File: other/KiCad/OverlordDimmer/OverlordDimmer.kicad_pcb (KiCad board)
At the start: 2 copper layers, 155.1 x 86.1 mm, 236 parts, among them J1 Connector_Screw_Terminal_01x09, J2 USB_B, J2 USB_cable, J3 DE15_Plug_HighDensity_Mountin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, J4 Connector_Screw_Terminal_01x09, J5 USB_B, J6 Conn_01x12_Pin, Q1 IRF740, Q10 IRF740, Q11 IRF740, Q12 IRF740, Q13 2N3906, Q14 IRF740, Q15 2N3904, Q16 IRF740, Q17 2N3906, Q18 2N3904, Q19 IRF740, Q2 2N3904, Q20 IRF740, Q21 2N7002E, Q22 2N7002E, Q23 2N3904, Q24 IRF740, Q25 IRF740, Q26 2N3904, Q27 IRF740, Q28 IRF740, Q29 2N3906, Q3 2N3906, Q30 2N3904, Q31 2N3906, Q32 IRF740, Q33 2N3906, Q34 2N3904, Q35 IRF740, Q36 IRF740, Q37 2N3904, Q38 2N3906, Q39 IRF740, Q4 IRF740, Q40 IRF740, Q41 2N3906, Q42 IRF740, Q43 2SC4061KT146N, Q44 BC817, Q45 2SC4061KT146N, Q5 IRF740, Q6 2N3906, Q7 2N3904, Q8 2N3904, Q9 2N3906, U1 4N25, U10 4N25, U11 4N25, U12 4N35, U13 LM317_SOT-223, U14 ESP32S3-Wroom, U2 4N25, U3 4N25, U4 SN65HVD230, U5 4N25, U6 4N25, U7 4N25, U8 4N25, U9 4N25

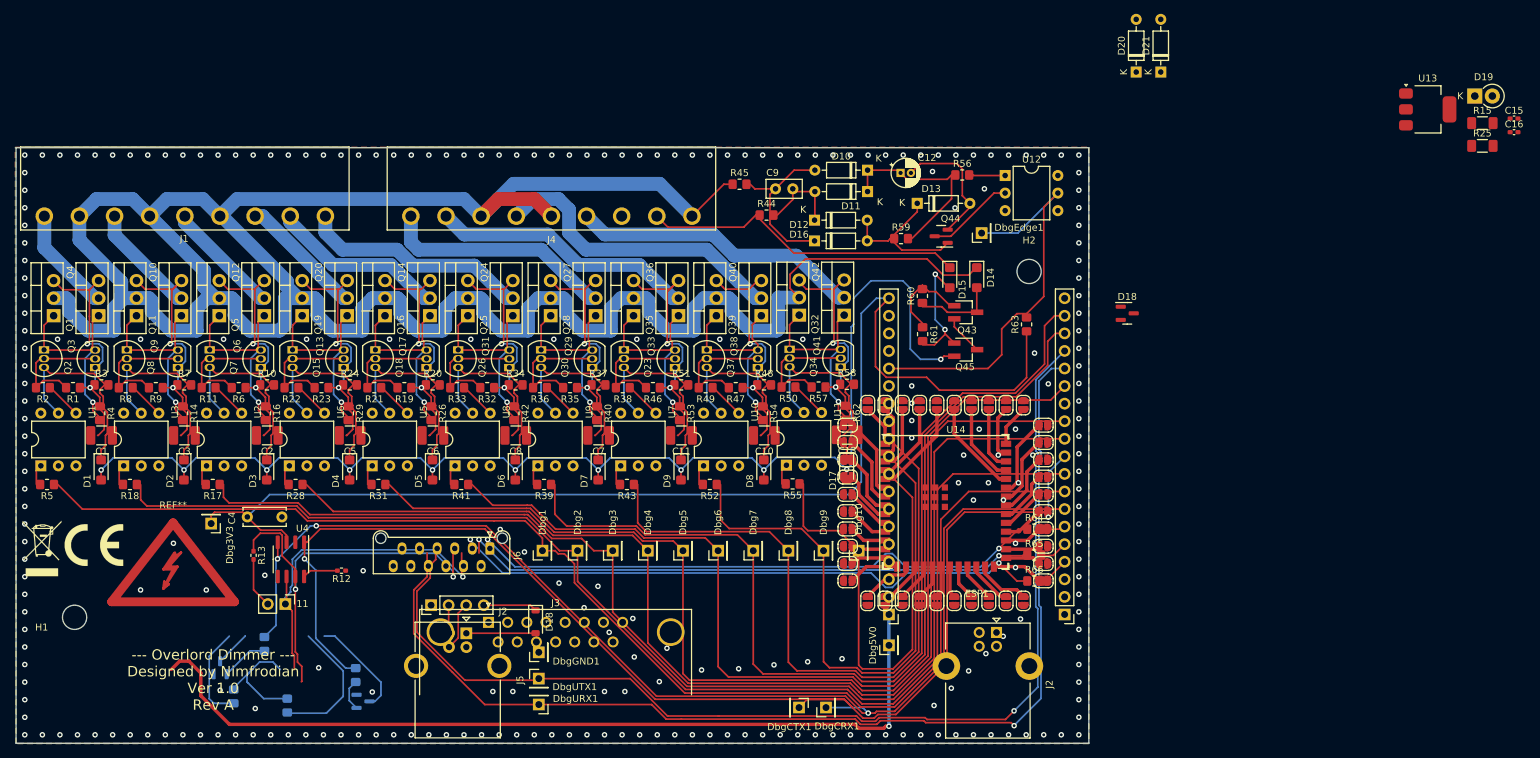
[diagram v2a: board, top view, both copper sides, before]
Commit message: Modified for S3 migration Prepared PCB for final inspection
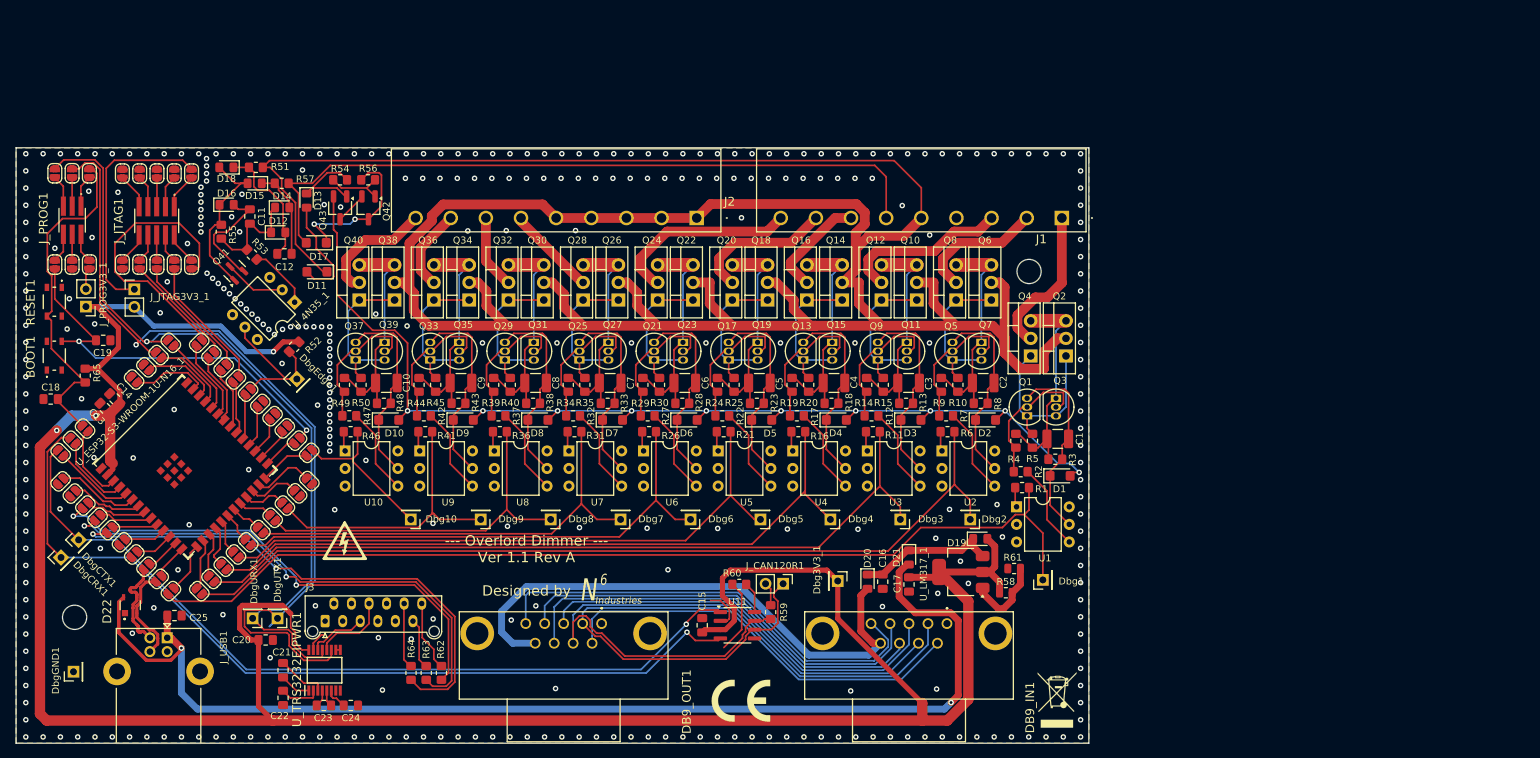
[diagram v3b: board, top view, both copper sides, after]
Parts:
- removed 11: Conn_01x02_Male, Connector_PinHeader_2.54mm:PinHeader_1x02_P2.54mm_Vertical
- removed the D18 at (186.2, 49.5)
- removed the D18 at (100.6, 94.1)
- removed Dbg3V3, Dbg5V0: Connector_Conn_01x01_Male, Connector_PinHeader_2.54mm:PinHeader_1x01_P2.54mm_Vertical
- removed ESP1: ESP-DevKitC-V4, Overlord:ESP32-DevKitC-V4
- removed the J2 at (167.2, 95.6)
- removed the J2 at (85.5, 91.7)
- removed J4: Connector_Screw_Terminal_01x09, TerminalBlockCustom:TerminalBlock_9_5.08mm
- removed J5: USB_B, Connector_USB:USB_B_OST_USB-B1HSxx_Horizontal
- removed J6: Conn_01x12_Pin, Connector_Molex:Molex_Picoflex_90325-0012_2x06_P1.27mm_Vertical
- removed JP1, JP2, JP3: SolderJumper_2_Open, Jumper:SolderJumper-2_P1.3mm_Open_RoundedPad1.0x1.5mm
- removed Q44: BC817, Package_TO_SOT_SMD:SOT-23
- removed Q45: 2SC4061KT146N, Package_TO_SOT_SMD:SC-59_Handsoldering
- removed the R15 at (237.5, 22.0)
- removed the R15 at (57.0, 104.9)
- removed the R25 at (237.5, 25.3)
- removed the R25 at (61.4, 97.3)
- removed R66: 220, Resistor_SMD:R_0805_2012Metric_Pad1.20x1.40mm_HandSolder
- removed REF**: CE-Logo_8.5x6mm_SilkScreen, Symbol:CE-Logo_8.5x6mm_SilkScreen
- removed REF**: Symbol_Highvoltage_Type2_CopperTop_Small, Symbol:Symbol_Highvoltage_Type2_CopperTop_Small
- removed REF**: WEEE-Logo_5.6x8mm_SilkScreen, Symbol:WEEE-Logo_5.6x8mm_SilkScreen
- removed U12: 4N35, Package_DIP:DIP-6_W7.62mm
- removed U13: LM317_SOT-223, Package_TO_SOT_SMD:SOT-223-3_TabPin2
- removed U14: ESP32S3-Wroom, PCM_Espressif:ESP32-S3-WROOM-1U
- added BOOT1: PTS810SJK250SMTR LFS, OverlordCommon:PTS810SJK250SMTRLFS, F.Cu at (31.0, 55.6)
- added C14: 10uF, Capacitor_SMD:C_0805_2012Metric_Pad1.18x1.45mm_HandSolder, F.Cu at (39.8, 61.8)
- added C17: 1uF, Capacitor_SMD:C_0805_2012Metric_Pad1.18x1.45mm_HandSolder, F.Cu at (154.6, 88.7)
- added C18: 0.1uF, Capacitor_SMD:C_0805_2012Metric_Pad1.18x1.45mm_HandSolder, F.Cu at (30.5, 61.9)
- added C19: 0.1uF, Capacitor_SMD:C_0805_2012Metric_Pad1.18x1.45mm_HandSolder, F.Cu at (38.1, 53.4)
- added C20: 0.1uF, Capacitor_SMD:C_0805_2012Metric_Pad1.18x1.45mm_HandSolder, F.Cu at (61.6, 96.7)
- added C21: 0.1uF, Capacitor_SMD:C_0805_2012Metric_Pad1.18x1.45mm_HandSolder, F.Cu at (64.1, 101.1)
- added C22: 0.1uF, Capacitor_SMD:C_0805_2012Metric_Pad1.18x1.45mm_HandSolder, F.Cu at (64.1, 105.1)
- added C23: 0.1uF, Capacitor_SMD:C_0805_2012Metric_Pad1.18x1.45mm_HandSolder, F.Cu at (70.0, 106.2)
- added C24: 0.1uF, Capacitor_SMD:C_0805_2012Metric_Pad1.18x1.45mm_HandSolder, F.Cu at (73.9, 106.2)
- added C25: 0.1uF, Capacitor_SMD:C_0805_2012Metric_Pad1.18x1.45mm_HandSolder, F.Cu at (48.4, 93.2)
- added D18: 1N4148, Diode_SMD:D_0805_2012Metric_Pad1.15x1.40mm_HandSolder, F.Cu at (55.9, 28.4)
- added D22: TPD2E001DZDR, OverlordCommon:TPD2E001DZDR, F.Cu at (42.0, 91.7)
- added DB9_IN1: 5788792-2, OverlordCommon:5788792, F.Cu at (154.6, 101.7)
- added DB9_OUT1: 5747844-4, OverlordCommon:57478444, F.Cu at (104.7, 101.7)
- added Dbg3V3_1: Connector_Conn_01x01_Male, Connector_PinHeader_2.54mm:PinHeader_1x01_P2.54mm_Vertical, F.Cu at (144.3, 88.2)
- added J2: 1757310, OverlordCommon:1757310, F.Cu at (123.9, 35.7)
- added JP41: SolderJumper_2_Open, Jumper:SolderJumper-2_P1.3mm_Open_RoundedPad1.0x1.5mm, F.Cu at (50.9, 29.3)
- added JP42: SolderJumper_2_Open, Jumper:SolderJumper-2_P1.3mm_Open_RoundedPad1.0x1.5mm, F.Cu at (50.9, 42.4)
- added JP43: SolderJumper_2_Open, Jumper:SolderJumper-2_P1.3mm_Open_RoundedPad1.0x1.5mm, F.Cu at (48.4, 29.3)
- added JP44: SolderJumper_2_Open, Jumper:SolderJumper-2_P1.3mm_Open_RoundedPad1.0x1.5mm, F.Cu at (48.4, 42.4)
- added JP45: SolderJumper_2_Open, Jumper:SolderJumper-2_P1.3mm_Open_RoundedPad1.0x1.5mm, F.Cu at (45.9, 29.3)
- added JP46: SolderJumper_2_Open, Jumper:SolderJumper-2_P1.3mm_Open_RoundedPad1.0x1.5mm, F.Cu at (45.9, 42.4)
- added JP47: SolderJumper_2_Open, Jumper:SolderJumper-2_P1.3mm_Open_RoundedPad1.0x1.5mm, F.Cu at (43.4, 29.3)
- added JP48: SolderJumper_2_Open, Jumper:SolderJumper-2_P1.3mm_Open_RoundedPad1.0x1.5mm, F.Cu at (43.4, 42.4)
- added JP49: SolderJumper_2_Open, Jumper:SolderJumper-2_P1.3mm_Open_RoundedPad1.0x1.5mm, F.Cu at (40.9, 29.3)
- added JP50: SolderJumper_2_Open, Jumper:SolderJumper-2_P1.3mm_Open_RoundedPad1.0x1.5mm, F.Cu at (40.9, 42.4)
- added JP51: SolderJumper_2_Open, Jumper:SolderJumper-2_P1.3mm_Open_RoundedPad1.0x1.5mm, F.Cu at (36.1, 29.2)
- added JP52: SolderJumper_2_Open, Jumper:SolderJumper-2_P1.3mm_Open_RoundedPad1.0x1.5mm, F.Cu at (36.1, 42.5)
- added JP53: SolderJumper_2_Open, Jumper:SolderJumper-2_P1.3mm_Open_RoundedPad1.0x1.5mm, F.Cu at (33.6, 29.2)
- added JP54: SolderJumper_2_Open, Jumper:SolderJumper-2_P1.3mm_Open_RoundedPad1.0x1.5mm, F.Cu at (33.6, 42.5)
- added JP55: SolderJumper_2_Open, Jumper:SolderJumper-2_P1.3mm_Open_RoundedPad1.0x1.5mm, F.Cu at (31.1, 29.2)
- added JP56: SolderJumper_2_Open, Jumper:SolderJumper-2_P1.3mm_Open_RoundedPad1.0x1.5mm, F.Cu at (31.1, 42.5)
- added J_CAN120R1: Conn_01x02_Male, Connector_PinHeader_2.54mm:PinHeader_1x02_P2.54mm_Vertical, F.Cu at (136.4, 88.6)
- added J_JTAG1: FTSH-105-01-S-DV-K, OverlordCommon:FTSH-105-XX-YYY-DV-K, F.Cu at (45.8, 36.1)
- added J_JTAG3V3_1: Conn_01x02_Pin, Connector_PinHeader_2.54mm:PinHeader_1x02_P2.54mm_Vertical, F.Cu at (42.6, 46.0)
- added J_PROG1: FTSH-103-01-S-DV-TR, OverlordCommon:FTSH-103-XX-YYY-DV-TR, F.Cu at (33.6, 36.0)
- added J_PROG3V3_1: Conn_01x02_Pin, Connector_PinHeader_2.54mm:PinHeader_1x02_P2.54mm_Vertical, F.Cu at (35.6, 48.5)
- added J_USB1: USB_B, Connector_USB:USB_B_Lumberg_2411_02_Horizontal, F.Cu at (47.4, 96.4)
- added R15: 470k, Resistor_SMD:R_0805_2012Metric_Pad1.20x1.40mm_HandSolder, F.Cu at (150.9, 59.8)
- added R25: 470k, Resistor_SMD:R_0805_2012Metric_Pad1.20x1.40mm_HandSolder, F.Cu at (129.3, 59.8)
- added RESET1: PTS810SJK250SMTR LFS, OverlordCommon:PTS810SJK250SMTRLFS, F.Cu at (31.0, 47.8)
- added SYM1: HV_symbol, OverlordCommon:HV_symbol, B.Cu at (160.8, 30.6)
- added SYM2: N6_logo_medium, OverlordCommon:Symbol_N6Industries_medium, B.Cu at (172.6, 106.3)
- added SYM3: CE, Symbol:CE-Logo_8.5x6mm_SilkScreen, F.Cu at (130.3, 105.5)
- added SYM4: WEEE, Symbol:WEEE-Logo_5.6x8mm_SilkScreen, F.Cu at (176.0, 105.4)
- added SYM5: N6_logo_medium, OverlordCommon:Symbol_N6Industries_medium, F.Cu at (111.7, 89.9)
- added SYM6: HV_symbol, OverlordCommon:HV_symbol, F.Cu at (73.0, 82.7)
- added U_4N35_1: 4N35, Package_DIP:DIP-6_W7.62mm, F.Cu at (65.8, 47.9)
- added U_ESP32-S3-WROOM-1U-N16_1: ESP32S3-Wroom, PCM_Espressif:ESP32-S3-WROOM-1U, F.Cu at (49.8, 71.6)
- added U_LM317_1: LM317_SOT-223, Package_TO_SOT_SMD:SOT-223-3_TabPin2, F.Cu at (162.1, 86.9)
- added U_TRS3232EIPWR1: TRS3232EIPWR, OverlordCommon:SOP65P640X120-16N, F.Cu at (70.1, 101.1)
- C11: value 4.7u -> 10uF; footprint Capacitor_SMD:C_1210_3225Metric_Pad1.33x2.70mm_HandSolder -> Capacitor_SMD:C_0805_2012Metric_Pad1.18x1.45mm_HandSolder
- C12: value 10uF -> 1nF; footprint Capacitor_THT:CP_Radial_D4.0mm_P1.50mm -> Capacitor_SMD:C_0805_2012Metric_Pad1.18x1.45mm_HandSolder
- C13: value 4.7u -> 0.1uF; footprint Capacitor_SMD:C_1210_3225Metric_Pad1.33x2.70mm_HandSolder -> Capacitor_SMD:C_0805_2012Metric_Pad1.18x1.45mm_HandSolder
- C15: value 1uF -> 0.1uF; footprint Capacitor_SMD:C_0402_1005Metric_Pad0.74x0.62mm_HandSolder -> Capacitor_SMD:C_0805_2012Metric_Pad1.18x1.45mm_HandSolder
- C16: footprint Capacitor_SMD:C_0402_1005Metric_Pad0.74x0.62mm_HandSolder -> Capacitor_SMD:C_0805_2012Metric_Pad1.18x1.45mm_HandSolder
- C4: value 100nF -> 4.7u; footprint Capacitor_THT:C_Disc_D6.0mm_W2.5mm_P5.00mm -> Capacitor_SMD:C_1210_3225Metric_Pad1.33x2.70mm_HandSolder
- C9: value 1nF -> 4.7u; footprint Capacitor_THT:C_Disc_D5.0mm_W2.5mm_P2.50mm -> Capacitor_SMD:C_1210_3225Metric_Pad1.33x2.70mm_HandSolder
- D10, D11: value 1N4148 -> VISHAY S07J-GS08; footprint Diode_THT:D_DO-35_SOD27_P7.62mm_Horizontal -> Diode_SMD:D_SMF
- D12, D16, D20, D21: footprint Diode_THT:D_DO-35_SOD27_P7.62mm_Horizontal -> Diode_SMD:D_0805_2012Metric_Pad1.15x1.40mm_HandSolder
- D13: value 1N4148 -> Unknown; footprint Diode_THT:D_DO-35_SOD27_P7.62mm_Horizontal -> Diode_SMD:D_0805_2012Metric_Pad1.15x1.40mm_HandSolder
- D14, D15: value VISHAY S07J-GS08 -> 1N4148; footprint Diode_SMD:D_SMF -> Diode_SMD:D_0805_2012Metric_Pad1.15x1.40mm_HandSolder
- D19: value 1N4002 -> 1N4148; footprint Diode_THT:D_DO-41_SOD81_P2.54mm_Vertical_KathodeUp -> Diode_SMD:D_0805_2012Metric_Pad1.15x1.40mm_HandSolder
- J1: value Connector_Screw_Terminal_01x09 -> 1757310; footprint TerminalBlockCustom:TerminalBlock_9_5.08mm -> OverlordCommon:1757310
- J3: value DE15_Plug_HighDensity_MountingHoles -> Conn_01x12_Pin; footprint Connector_Dsub:DSUB-15_Male_Horizontal_P2.77x2.84mm_EdgePinOffset7.70mm_Housed_MountingHolesOffset9.12mm -> Connector_Molex:Molex_Picoflex_90325-0012_2x06_P1.27mm_Vertical
- Q1, Q25, Q5: value IRF740 -> 2N3904; footprint Package_TO_SOT_THT:TO-220-3_Vertical -> Package_TO_SOT_THT:TO-92_Inline
- Q11, Q19, Q27, Q35, Q39: value IRF740 -> 2N3906; footprint Package_TO_SOT_THT:TO-220-3_Vertical -> Package_TO_SOT_THT:TO-92_Inline
- Q13, Q17, Q29, Q33, Q9: value 2N3906 -> 2N3904
- Q15, Q23, Q7: value 2N3904 -> 2N3906
- Q18, Q2, Q26, Q30, Q34, Q8: value 2N3904 -> IRF740; footprint Package_TO_SOT_THT:TO-92_Inline -> Package_TO_SOT_THT:TO-220-3_Vertical
- Q21: value 2N7002E -> 2N3904; footprint Package_TO_SOT_SMD:SOT-23 -> Package_TO_SOT_THT:TO-92_Inline; moved to F.Cu
- Q22: value 2N7002E -> IRF740; footprint Package_TO_SOT_SMD:SOT-23 -> Package_TO_SOT_THT:TO-220-3_Vertical; moved to F.Cu
- Q38, Q6: value 2N3906 -> IRF740; footprint Package_TO_SOT_THT:TO-92_Inline -> Package_TO_SOT_THT:TO-220-3_Vertical
- Q41: value 2N3906 -> BC817; footprint Package_TO_SOT_THT:TO-92_Inline -> Package_TO_SOT_SMD:SOT-23
- Q42: value IRF740 -> 2SC4061KT146N; footprint Package_TO_SOT_THT:TO-220-3_Vertical -> Package_TO_SOT_SMD:SC-59_Handsoldering
- R1, R46, R6: value 10k -> 220
- R11, R21, R36: value 1k -> 220
- R12: value 20K -> 1k; footprint Resistor_SMD:R_0402_1005Metric_Pad0.72x0.64mm_HandSolder -> Resistor_SMD:R_0805_2012Metric_Pad1.20x1.40mm_HandSolder
- R13: value 120 -> 470k; footprint Resistor_SMD:R_0402_1005Metric_Pad0.72x0.64mm_HandSolder -> Resistor_SMD:R_0805_2012Metric_Pad1.20x1.40mm_HandSolder
- R14, R24, R29, R34, R4: value 470k -> 10k
- R16, R26, R62: value 470k -> 220
- R17: value 220 -> 1k
- R18, R28, R43, R5: value 220 -> 470k
- R23, R35: value 10k -> 470k
- R27: value 5K -> 1k; moved to F.Cu
- R30: value 10K -> 470k; moved to F.Cu
- R32, R47: value 10k -> 1k
- R33, R38, R50, R8: value 1k -> 470k
- R37, R42, R53, R7: value 470k -> 1k
- R39, R65: value 220 -> 10k
- R44: value 220k -> 10k
- R45: value 220k -> 470k
- R49: value 1k -> 10k
- R51: value 470k -> 220k
- R52: value 220 -> 2.2k
- R54: value 470k -> 100k
- R55: value 220 -> 22k
- R56: value 1k -> 75k
- R57: value 10k -> 220k
- R58: value 470k -> 240; footprint Resistor_SMD:R_0805_2012Metric_Pad1.20x1.40mm_HandSolder -> Resistor_SMD:R_0805_2012Metric
- R59: value 22k -> 120
- R60: value 75k -> 0R
- R61: value 100k -> 390; footprint Resistor_SMD:R_0805_2012Metric_Pad1.20x1.40mm_HandSolder -> Resistor_SMD:R_0805_2012Metric
- R63: value 2.2k -> 220
- U11: value 4N25 -> SN65HVD230; footprint Package_DIP:DIP-6_W7.62mm -> Package_SO:SOIC-8_3.9x4.9mm_P1.27mm
- U4: value SN65HVD230 -> 4N25; footprint Package_SO:SOIC-8_3.9x4.9mm_P1.27mm -> Package_DIP:DIP-6_W7.62mm
- moved Q2 147.8 mm to (177.3, 55.7), turned to 90 degrees
- moved R5 142.6 mm to (172.4, 67.9), turned to 90 degrees
- moved JP11 142.2 mm to (31.9, 73.8), turned to -135 degrees
- moved JP9 142.1 mm to (31.9, 69.7), turned to 135 degrees
- moved R2 141.9 mm to (170.8, 72.4)
- moved Q1 141.5 mm to (171.7, 64.3)
- moved U1 141.2 mm to (170.2, 77.5), turned to 0 degrees
- moved JP13 140.5 mm to (33.7, 75.6), turned to -135 degrees
- moved JP7 140.3 mm to (33.7, 67.9), turned to 135 degrees
- moved R65 139.6 mm to (35.5, 58.5), turned to 90 degrees
- moved Q3 139.0 mm to (175.8, 61.8), turned to -90 degrees
- moved D1 138.7 mm to (176.4, 73.0), turned to 0 degrees
- moved C15 138.4 mm to (124.7, 94.6), turned to 90 degrees
- moved R3 138.3 mm to (175.8, 70.6)
- moved C1 138.3 mm to (176.1, 67.7)
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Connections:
- C1 pad 2: Net-(Q1-S) -> Net-(Q2-S)
- C10 pad 1: Net-(D8-K) -> Net-(D10-K)
- C10 pad 2: Net-(Q38-E) -> Net-(Q38-S)
- C11 pad 1: Net-(D9-K) -> Net-(D12-K)
- C11 pad 2: Net-(Q33-E) -> Net-(D16-A)
- C12 pad 1: Net-(D10-K) -> Net-(D12-A)
- C12 pad 2: Net-(D13-A) -> Net-(D14-A)
- C13 pad 1: Net-(D17-K) -> +3.3V
- C13 pad 2: Net-(Q32-S) -> GND
- C15 pad 1: Net-(D19-K) -> +3.3V
- C16 pad 1: +3.3V -> Net-(D19-K)
- C2 pad 1: Net-(D3-K) -> Net-(D2-K)
- C2 pad 2: Net-(Q12-S) -> Net-(Q6-S)
- C3 pad 1: Net-(D2-K) -> Net-(D3-K)
- C4 pad 1: GND -> Net-(D4-K)
- C4 pad 2: +3.3V -> Net-(Q14-S)
- C5 pad 1: Net-(D4-K) -> Net-(D5-K)
- C5 pad 2: Net-(Q13-E) -> Net-(Q18-S)
- C6 pad 1: Net-(D5-K) -> Net-(D6-K)
- C6 pad 2: Net-(Q14-S) -> Net-(Q22-S)
- C7 pad 2: Net-(Q27-S) -> Net-(Q26-S)
- C8 pad 1: Net-(D6-K) -> Net-(D8-K)
- C8 pad 2: Net-(Q24-S) -> Net-(Q30-S)
- C9 pad 1: Net-(D10-A) -> Net-(D9-K)
- C9 pad 2: Net-(D11-A) -> Net-(Q34-S)
- D10 pad 2: Net-(D10-A) -> VCC
- D11 pad 1: Net-(D10-K) -> L
- D12 pad 1: Net-(D11-A) -> Net-(D12-K)
- D13 pad 1: Net-(D12-A) -> Net-(D13-K)
- D13 pad 2: Net-(D13-A) -> Net-(D11-A)
- D14 pad 1: L -> Net-(D12-K)
- D15 pad 1: Net-(D15-K) -> Net-(D14-A)
- D15 pad 2: N -> Net-(D15-A)
- D16 pad 1: Net-(D10-A) -> Net-(D15-A)
- D16 pad 2: Net-(D12-A) -> Net-(D16-A)
- D17 pad 2: VCC -> N
- J1 pad 1: /Load -> OUT1
- J1 pad 2: /Load_8 -> OUT2
- J1 pad 3: /Load_6 -> OUT3
- J1 pad 4: unconnected-(J1-Pin_4-Pad4) -> GND
- J1 pad 5: /Load_7 -> L
- J1 pad 6: unconnected-(J1-Pin_6-Pad6) -> N
- J1 pad 7: /Load_5 -> OUT4
- J1 pad 8: unconnected-(J1-Pin_8-Pad8) -> OUT5
- J1 pad 9: /Load_9 -> OUT6
- J3 pad 1: GND -> unconnected-(J3-Pin_1-Pad1)
- J3 pad 10: unconnected-(J3-Pad10) -> Net-(J3-Pin_10)
- J3 pad 11: CAN_H -> Net-(J3-Pin_11)
- J3 pad 12: MB1_H -> Net-(J3-Pin_12)
- J3 pad 2: MB1_L -> unconnected-(J3-Pin_2-Pad2)
- J3 pad 5: unconnected-(J3-Pad5) -> RS232_TX
- J3 pad 6: GND -> RS232_RX
- J3 pad 7: CAN_L -> GND
- J3 pad 8: MB2_L -> unconnected-(J3-Pin_8-Pad8)
- JP10 pad 2: unconnected-(JP10-B-Pad2) -> UART_RX_0
- JP12 pad 2: unconnected-(JP12-B-Pad2) -> JTAG_TMS
- JP14 pad 2: unconnected-(JP14-B-Pad2) -> JTAG_TDI
- JP15 pad 2: unconnected-(JP15-B-Pad2) -> STATUS_LED_R
- JP16 pad 2: unconnected-(JP16-B-Pad2) -> JTAG_TDO
- JP17 pad 2: unconnected-(JP17-B-Pad2) -> STATUS_LED_G
- JP18 pad 2: unconnected-(JP18-B-Pad2) -> JTAG_TCK
- JP19 pad 2: unconnected-(JP19-B-Pad2) -> STATUS_LED_B
- JP20 pad 2: unconnected-(JP20-B-Pad2) -> EDGE_DETECT
- JP25 pad 2: unconnected-(JP25-B-Pad2) -> D-
- JP27 pad 2: unconnected-(JP27-B-Pad2) -> D+
- JP28 pad 2: unconnected-(JP28-B-Pad2) -> ESP_IO0
- JP29 pad 2: unconnected-(JP29-B-Pad2) -> TRGR1
- JP30 pad 2: unconnected-(JP30-B-Pad2) -> TRGR2
- JP31 pad 2: unconnected-(JP31-B-Pad2) -> TRGR3
- JP32 pad 2: unconnected-(JP32-B-Pad2) -> TRGR4
- JP33 pad 2: unconnected-(JP33-B-Pad2) -> TRGR5
- JP34 pad 2: unconnected-(JP34-B-Pad2) -> TRGR6
- JP35 pad 2: unconnected-(JP35-B-Pad2) -> TRGR7
- JP36 pad 2: unconnected-(JP36-B-Pad2) -> TRGR8
- JP37 pad 2: unconnected-(JP37-B-Pad2) -> TRGR9
- JP40 pad 2: unconnected-(JP40-B-Pad2) -> TRGR10
- JP5 pad 2: unconnected-(JP5-B-Pad2) -> ESP_EN
- JP7 pad 2: unconnected-(JP7-B-Pad2) -> CAN_RX
- JP8 pad 2: unconnected-(JP8-B-Pad2) -> UART_TX_0
- JP9 pad 2: unconnected-(JP9-B-Pad2) -> CAN_TX
- Q1 pad 1: Net-(Q1-G) -> Net-(Q1-E)
- Q1 pad 2: L -> Net-(Q1-B)
- Q1 pad 3: Net-(Q1-S) -> Net-(D1-K)
- Q10 pad 2: Load -> L
- Q11 pad 1: Net-(Q10-G) -> Net-(Q10-S)
- Q11 pad 2: L -> Net-(Q11-B)
- Q11 pad 3: Net-(Q10-S) -> Net-(Q10-G)
- Q12 pad 1: Net-(Q12-G) -> Net-(Q10-G)
- Q12 pad 2: Load -> OUT3
- Q12 pad 3: Net-(Q12-S) -> Net-(Q10-S)
- Q13 pad 3: Net-(Q13-C) -> Net-(D4-K)
- Q14 pad 1: Net-(Q14-G) -> Net-(Q13-E)
- Q14 pad 2: Load -> L
- Q15 pad 1: Net-(Q13-C) -> Net-(Q14-S)
- Q15 pad 3: Net-(D4-K) -> Net-(Q13-E)
- Q16 pad 1: Net-(Q14-G) -> Net-(Q13-E)
- Q16 pad 2: L -> OUT4
- Q17 pad 1: Net-(Q14-S) -> Net-(Q17-E)
- Q17 pad 3: Net-(Q14-G) -> Net-(D5-K)
- Q18 pad 1: Net-(Q14-G) -> Net-(Q17-E)
- Q18 pad 2: Net-(Q17-B) -> L
- Q18 pad 3: Net-(D5-K) -> Net-(Q18-S)
- Q19 pad 1: Net-(Q13-C) -> Net-(Q18-S)
- Q19 pad 2: L -> Net-(Q17-B)
- Q19 pad 3: Net-(Q13-E) -> Net-(Q17-E)
- Q2 pad 1: Net-(Q1-G) -> Net-(Q1-E)
- Q2 pad 2: Net-(Q2-B) -> L
- Q2 pad 3: Net-(D1-K) -> Net-(Q2-S)
- Q20 pad 1: Net-(Q13-C) -> Net-(Q17-E)
- Q20 pad 2: Load -> OUT5
- Q20 pad 3: Net-(Q13-E) -> Net-(Q18-S)
- Q21 pad 1: Net-(Q21-G) -> Net-(Q21-E)
- Q21 pad 2: GND -> Net-(Q21-B)
- Q21 pad 3: Net-(Q21-D) -> Net-(D6-K)
- Q22 pad 1: Net-(Q22-G) -> Net-(Q21-E)
- Q22 pad 2: GND -> L
- Q22 pad 3: Net-(Q22-D) -> Net-(Q22-S)
- Q23 pad 1: Net-(Q23-E) -> Net-(Q22-S)
- Q23 pad 2: Net-(Q23-B) -> Net-(Q21-B)
- Q23 pad 3: Net-(D9-K) -> Net-(Q21-E)
- Q24 pad 1: Net-(Q24-G) -> Net-(Q21-E)
- Q24 pad 2: Load -> OUT6
- Q24 pad 3: Net-(Q24-S) -> Net-(Q22-S)
- Q25 pad 1: Net-(Q24-G) -> Net-(Q25-E)
- Q25 pad 2: L -> Net-(Q25-B)
- Q25 pad 3: Net-(Q24-S) -> Net-(D7-K)
- Q26 pad 1: Net-(Q24-G) -> Net-(Q25-E)
- Q26 pad 2: Net-(Q26-B) -> L
- Q26 pad 3: Net-(D6-K) -> Net-(Q26-S)
- Q27 pad 1: Net-(Q27-G) -> Net-(Q26-S)
- Q27 pad 2: Load -> Net-(Q25-B)
- Q27 pad 3: Net-(Q27-S) -> Net-(Q25-E)
- Q28 pad 1: Net-(Q27-G) -> Net-(Q25-E)
- Q28 pad 2: L -> OUT7
- Q28 pad 3: Net-(Q27-S) -> Net-(Q26-S)
- Q29 pad 1: Net-(Q27-S) -> Net-(Q29-E)
- Q29 pad 3: Net-(Q27-G) -> Net-(D8-K)
- Q3 pad 1: Net-(Q1-S) -> Net-(Q2-S)
- Q3 pad 2: Net-(Q2-B) -> Net-(Q1-B)
- Q3 pad 3: Net-(Q1-G) -> Net-(Q1-E)
- Q30 pad 1: Net-(Q27-G) -> Net-(Q29-E)
- Q30 pad 2: Net-(Q29-B) -> L
- Q30 pad 3: Net-(D7-K) -> Net-(Q30-S)
- Q31 pad 1: Net-(Q24-S) -> Net-(Q30-S)
- Q31 pad 2: Net-(Q26-B) -> Net-(Q29-B)
- Q31 pad 3: Net-(Q24-G) -> Net-(Q29-E)
- Q32 pad 1: Net-(Q32-G) -> Net-(Q29-E)
- Q32 pad 2: L -> OUT8
- Q32 pad 3: Net-(Q32-S) -> Net-(Q30-S)
- Q33 pad 2: Net-(Q23-B) -> Net-(Q33-B)
- Q33 pad 3: Net-(Q23-E) -> Net-(D9-K)
- Q34 pad 1: Net-(Q32-G) -> Net-(Q33-E)
- Q34 pad 2: Net-(Q34-B) -> L
- Q34 pad 3: Net-(D17-K) -> Net-(Q34-S)
- Q35 pad 1: Net-(Q23-E) -> Net-(Q34-S)
- Q35 pad 2: L -> Net-(Q33-B)
- Q36 pad 1: Net-(Q23-E) -> Net-(Q33-E)
- Q36 pad 2: Load -> OUT9
- Q36 pad 3: Net-(Q33-E) -> Net-(Q34-S)
- Q37 pad 3: Net-(D8-K) -> Net-(D10-K)
- Q38 pad 1: Net-(Q38-E) -> Net-(Q37-E)
- Q38 pad 2: Net-(Q37-B) -> L
- Q38 pad 3: Net-(Q37-E) -> Net-(Q38-S)
- Q39 pad 1: Net-(Q37-E) -> Net-(Q38-S)
- Q39 pad 2: L -> Net-(Q37-B)
- Q39 pad 3: Net-(Q38-E) -> Net-(Q37-E)
- Q4 pad 1: Net-(Q1-G) -> Net-(Q1-E)
- Q4 pad 2: Load -> OUT1
- Q4 pad 3: Net-(Q1-S) -> Net-(Q2-S)
- Q40 pad 2: Load -> OUT10
- Q40 pad 3: Net-(Q38-E) -> Net-(Q38-S)
- Q41 pad 1: Net-(Q32-S) -> Net-(D15-A)
- Q41 pad 2: Net-(Q34-B) -> Net-(D16-A)
- Q41 pad 3: Net-(Q32-G) -> Net-(Q41-C)
- Q42 pad 1: Net-(Q32-G) -> Net-(Q42-B)
- Q42 pad 2: Load -> Net-(Q42-E)
- Q42 pad 3: Net-(Q32-S) -> Net-(D17-K)
- Q43 pad 1: Net-(Q43-B) -> Net-(D13-K)
- Q43 pad 2: Net-(Q43-E) -> VCC
- Q43 pad 3: Net-(D15-K) -> Net-(Q42-E)
- Q5 pad 1: Net-(Q12-G) -> Net-(Q5-E)
- Q5 pad 2: L -> Net-(Q5-B)
- Q5 pad 3: Net-(Q12-S) -> Net-(D2-K)
- Q6 pad 1: Net-(Q12-S) -> Net-(Q5-E)
- Q6 pad 2: Net-(Q6-B) -> L
- Q6 pad 3: Net-(Q12-G) -> Net-(Q6-S)
- Q7 pad 1: Net-(Q12-G) -> Net-(Q6-S)
- Q7 pad 2: Net-(Q6-B) -> Net-(Q5-B)
- Q7 pad 3: Net-(D3-K) -> Net-(Q5-E)
- Q8 pad 1: Net-(Q10-G) -> Net-(Q5-E)
- Q8 pad 2: Net-(Q8-B) -> OUT2
- Q8 pad 3: Net-(D2-K) -> Net-(Q6-S)
- Q9 pad 1: Net-(Q10-S) -> Net-(Q10-G)
- Q9 pad 2: Net-(Q8-B) -> Net-(Q11-B)
- Q9 pad 3: Net-(Q10-G) -> Net-(D3-K)
- R1 pad 1: Net-(Q1-S) -> TRGR1
- R1 pad 2: Net-(Q2-B) -> Net-(R1-Pad2)
- R10 pad 1: Net-(Q12-S) -> Net-(Q6-S)
- R10 pad 2: Net-(D3-K) -> Net-(Q5-E)
- R11 pad 1: Net-(R11-Pad1) -> TRGR3
- R11 pad 2: Net-(Q6-B) -> Net-(R11-Pad2)
- R12 pad 1: GND -> Net-(R12-Pad1)
- R12 pad 2: Net-(U4-Rs) -> Net-(Q11-B)
- R13 pad 1: CAN_H -> Net-(Q10-S)
- R13 pad 2: Net-(11-Pin_2) -> Net-(D3-K)
- R14 pad 2: Net-(Q10-G) -> Net-(Q11-B)
- R16 pad 1: Net-(Q12-S) -> TRGR4
- R16 pad 2: Net-(Q12-G) -> Net-(R16-Pad2)
- R17 pad 1: TRGR3 -> Net-(R17-Pad1)
- R17 pad 2: Net-(R17-Pad2) -> Net-(Q13-B)
- R18 pad 1: TRGR2 -> Net-(Q14-S)
- R18 pad 2: Net-(R18-Pad2) -> Net-(D4-K)
- R19 pad 2: Net-(Q17-B) -> Net-(Q13-B)
- R2 pad 2: Net-(Q2-B) -> Net-(Q1-B)
- R20 pad 2: Net-(D5-K) -> Net-(Q13-E)
- R21 pad 1: Net-(R21-Pad1) -> TRGR5
- R21 pad 2: Net-(Q17-B) -> Net-(R21-Pad2)
- R22 pad 2: Net-(Q13-B) -> Net-(Q17-B)
- R23 pad 1: Net-(Q13-E) -> Net-(Q18-S)
- R23 pad 2: Net-(Q13-B) -> Net-(D5-K)
- R24 pad 1: Net-(Q13-E) -> Net-(Q18-S)
- R24 pad 2: Net-(D4-K) -> Net-(Q17-B)
- R26 pad 1: Net-(Q14-S) -> TRGR6
- R26 pad 2: Net-(Q14-G) -> Net-(R26-Pad2)
- R27 pad 1: Net-(J3-Pad10) -> Net-(R27-Pad1)
- R27 pad 2: +12V -> Net-(Q21-B)
- R28 pad 1: TRGR4 -> Net-(Q22-S)
- R28 pad 2: Net-(R28-Pad2) -> Net-(D6-K)
- R29 pad 1: Net-(Q13-E) -> Net-(Q22-S)
- R29 pad 2: Net-(Q13-C) -> Net-(Q21-B)
- R3 pad 1: Net-(Q1-S) -> Net-(Q2-S)
- R30 pad 1: Net-(Q21-G) -> Net-(Q22-S)
- R30 pad 2: CAN_TX -> Net-(Q21-E)
- R31 pad 1: TRGR5 -> TRGR7
- R32 pad 1: Net-(Q24-S) -> Net-(R32-Pad1)
- R32 pad 2: Net-(Q26-B) -> Net-(Q25-B)
- R33 pad 1: Net-(R33-Pad1) -> Net-(Q26-S)
- R33 pad 2: Net-(Q26-B) -> Net-(D7-K)
- R34 pad 1: Net-(Q24-S) -> Net-(Q26-S)
- R34 pad 2: Net-(D6-K) -> Net-(Q25-B)
- R35 pad 1: Net-(Q27-S) -> Net-(Q26-S)
- R35 pad 2: Net-(Q29-B) -> Net-(Q25-E)
- R36 pad 1: Net-(R36-Pad1) -> TRGR8
- R36 pad 2: Net-(Q29-B) -> Net-(R36-Pad2)
- R37 pad 1: Net-(Q27-S) -> Net-(R37-Pad1)
- R37 pad 2: Net-(D7-K) -> Net-(Q29-B)
- R38 pad 1: Net-(R38-Pad1) -> Net-(Q30-S)
- R38 pad 2: Net-(Q23-B) -> Net-(D8-K)
- R39 pad 1: TRGR7 -> Net-(Q30-S)
- R39 pad 2: Net-(R39-Pad2) -> Net-(Q29-B)
- R4 pad 1: Net-(Q1-S) -> Net-(Q2-S)
- R4 pad 2: Net-(Q1-G) -> Net-(Q1-B)
- R40 pad 1: Net-(Q27-S) -> Net-(Q30-S)
- R40 pad 2: Net-(Q27-G) -> Net-(Q29-E)
- R41 pad 1: TRGR6 -> TRGR9
- R42 pad 1: Net-(Q24-S) -> Net-(R42-Pad1)
- R42 pad 2: Net-(Q24-G) -> Net-(Q33-B)
- R43 pad 1: TRGR8 -> Net-(Q34-S)
- R43 pad 2: Net-(R43-Pad2) -> Net-(D9-K)
- R44 pad 1: N -> Net-(Q34-S)
- R44 pad 2: Net-(D11-A) -> Net-(Q33-B)
- R45 pad 1: L -> Net-(Q34-S)
- R45 pad 2: Net-(D10-A) -> Net-(Q33-E)
- R46 pad 1: Net-(Q33-E) -> TRGR10
- R46 pad 2: Net-(Q23-B) -> Net-(R46-Pad2)
- R47 pad 1: Net-(Q38-E) -> Net-(R47-Pad1)
- R48 pad 1: Net-(Q38-E) -> Net-(Q38-S)
- R48 pad 2: Net-(D8-K) -> Net-(D10-K)
- R49 pad 1: Net-(R49-Pad1) -> Net-(Q38-S)
- R5 pad 1: TRGR1 -> Net-(Q2-S)
- R5 pad 2: Net-(R5-Pad2) -> Net-(Q1-E)
- R50 pad 1: Net-(R50-Pad1) -> Net-(Q38-S)
- R50 pad 2: Net-(Q34-B) -> Net-(Q37-E)
- R51 pad 1: Net-(Q33-E) -> L
- R51 pad 2: Net-(D9-K) -> Net-(D12-A)
- R52 pad 1: TRGR9 -> +3.3V
- R52 pad 2: Net-(R52-Pad2) -> EDGE_DETECT
- R53 pad 1: Net-(Q33-E) -> Net-(D12-K)
- R53 pad 2: Net-(Q23-E) -> Net-(R53-Pad2)
- R54 pad 1: Net-(Q38-E) -> Net-(D13-K)
- R54 pad 2: Net-(Q37-E) -> Net-(Q42-B)
- R55 pad 1: TRGR10 -> Net-(D15-A)
- R55 pad 2: Net-(R55-Pad2) -> Net-(D12-K)
- R56 pad 1: Net-(D10-K) -> Net-(Q42-B)
- R56 pad 2: Net-(R56-Pad2) -> Net-(D17-K)
- R57 pad 1: Net-(Q32-S) -> N
- R57 pad 2: Net-(Q34-B) -> Net-(D14-A)
- R58 pad 1: Net-(Q32-S) -> +3.3V
- R58 pad 2: Net-(D17-K) -> Net-(U_LM317_1-ADJ)
- R59 pad 1: Net-(D12-A) -> CAN_H
- R59 pad 2: Net-(D10-K) -> Net-(J_CAN120R1-Pin_2)
- R6 pad 1: Net-(Q12-S) -> TRGR2
- R6 pad 2: Net-(Q6-B) -> Net-(R6-Pad2)
- R60 pad 1: Net-(Q43-B) -> GND
- R60 pad 2: Net-(D15-K) -> Net-(U11-Rs)
- R61 pad 1: Net-(D18-K) -> Net-(U_LM317_1-ADJ)
- R61 pad 2: Net-(Q43-B) -> GND
- R62 pad 1: Net-(Q32-S) -> Net-(J3-Pin_12)
- R62 pad 2: Net-(Q32-G) -> STATUS_LED_R
- R63 pad 1: +3.3V -> Net-(J3-Pin_11)
- R63 pad 2: EDGE_DETECT -> STATUS_LED_G
- R64 pad 1: Net-(J6-Pin_1) -> Net-(J3-Pin_10)
- R65 pad 1: Net-(J6-Pin_2) -> ESP_EN
- R65 pad 2: STATUS_LED_G -> +3.3V
- R7 pad 1: Net-(Q10-S) -> Net-(R7-Pad1)
- R7 pad 2: Net-(D2-K) -> Net-(Q5-B)
- R8 pad 1: Net-(R8-Pad1) -> Net-(Q6-S)
- R8 pad 2: Net-(Q8-B) -> Net-(D2-K)
- R9 pad 1: Net-(Q10-S) -> Net-(Q6-S)
- R9 pad 2: Net-(Q8-B) -> Net-(Q5-B)
- U1 pad 1: Net-(R5-Pad2) -> Net-(R1-Pad2)
- U10 pad 1: Net-(R52-Pad2) -> Net-(R46-Pad2)
- U10 pad 4: Net-(R49-Pad1) -> Net-(R47-Pad1)
- U10 pad 5: Net-(D8-K) -> Net-(D10-K)
- U11 pad 1: Net-(R55-Pad2) -> CAN_TX
- U11 pad 3: unconnected-(U11-NC-Pad3) -> +3.3V
- U11 pad 4: Net-(R50-Pad1) -> CAN_RX
- U11 pad 5: Net-(D17-K) -> unconnected-(U11-Vref-Pad5)
- U11 pad 6: unconnected-(U11-Pad6) -> CAN_L
- U2 pad 1: Net-(R17-Pad2) -> Net-(R6-Pad2)
- U2 pad 4: Net-(R11-Pad1) -> Net-(R7-Pad1)
- U2 pad 5: Net-(D3-K) -> Net-(D2-K)
- U3 pad 1: Net-(R18-Pad2) -> Net-(R11-Pad2)
- U3 pad 4: Net-(R8-Pad1) -> Net-(R12-Pad1)
- U3 pad 5: Net-(D2-K) -> Net-(D3-K)
- U4 pad 1: CAN_TX -> Net-(R16-Pad2)
- U4 pad 3: +3.3V -> unconnected-(U4-NC-Pad3)
- U4 pad 4: CAN_RX -> Net-(R17-Pad1)
- U4 pad 5: unconnected-(U4-Vref-Pad5) -> Net-(D4-K)
- U4 pad 6: CAN_L -> unconnected-(U4-Pad6)
- U5 pad 1: Net-(R31-Pad2) -> Net-(R21-Pad2)
- U5 pad 4: Net-(R21-Pad1) -> Net-(R22-Pad1)
- U6 pad 1: Net-(R28-Pad2) -> Net-(R26-Pad2)
- U6 pad 4: Net-(R22-Pad1) -> Net-(R27-Pad1)
- U6 pad 5: Net-(D4-K) -> Net-(D6-K)
- U7 pad 1: Net-(R43-Pad2) -> Net-(R31-Pad2)
- U7 pad 4: Net-(R38-Pad1) -> Net-(R32-Pad1)
- U7 pad 5: Net-(D9-K) -> Net-(D7-K)
- U8 pad 1: Net-(R41-Pad2) -> Net-(R36-Pad2)
- U8 pad 4: Net-(R33-Pad1) -> Net-(R37-Pad1)
- U8 pad 5: Net-(D6-K) -> Net-(D8-K)
- U9 pad 1: Net-(R39-Pad2) -> Net-(R41-Pad2)
- U9 pad 4: Net-(R36-Pad1) -> Net-(R42-Pad1)
- U9 pad 5: Net-(D7-K) -> Net-(D9-K)
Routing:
- net (no net): track 315.2 -> 0.00 mm
- net +3.3V: track 175.6 -> 383.8 mm, vias 0 -> 3
- net Net-(J6-Pin_3): track 88.0 -> 0.00 mm, vias 2 -> 0
- net Net-(J6-Pin_1): track 85.4 -> 0.00 mm, vias 2 -> 0
- net Net-(J6-Pin_2): track 84.4 -> 0.00 mm, vias 2 -> 0
- net TRGR7: track 141.3 -> 64.8 mm
- net STATUS_LED_B: track 3.55 -> 76.1 mm, vias 0 -> 2
- net TRGR6: track 149.3 -> 77.3 mm
- net STATUS_LED_G: track 4.17 -> 74.3 mm, vias 0 -> 2
- net TRGR5: track 157.2 -> 89.7 mm
- net STATUS_LED_R: track 4.55 -> 72.0 mm, vias 0 -> 2
- net MB2_H: track 0.00 -> 66.0 mm
- net CAN_TX: track 184.3 -> 119.5 mm, vias 2 -> 1
- net TRGR4: track 165.0 -> 102.5 mm
- net MB2_L: track 0.00 -> 62.0 mm
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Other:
- board text added: "--- Overlord Dimmer --- Ver 1.1 Rev A Designed by"
- board text removed: "--- Overlord Dimmer --- Designed by Nimfrodian Ver 1.0 Rev A"

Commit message: sent to production
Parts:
- added 12VLED1: LED, LED_SMD:LED_0805_2012Metric_Pad1.15x1.40mm_HandSolder, F.Cu at (176.6, 93.0)
- added 3V3LED1: LED, LED_SMD:LED_0805_2012Metric_Pad1.15x1.40mm_HandSolder, F.Cu at (176.6, 96.5)
- added 5VLED1: LED, LED_SMD:LED_0805_2012Metric_Pad1.15x1.40mm_HandSolder, F.Cu at (176.6, 89.6)
- added R61: 60, Resistor_SMD:R_0805_2012Metric_Pad1.20x1.40mm_HandSolder, F.Cu at (172.8, 96.5)
- added R67: 499, Resistor_SMD:R_0805_2012Metric_Pad1.20x1.40mm_HandSolder, F.Cu at (172.8, 93.0)
- added R68: 147, Resistor_SMD:R_0805_2012Metric_Pad1.20x1.40mm_HandSolder, F.Cu at (172.8, 89.7)
- D13: value Unknown -> BZY55B12 RBG
- moved Dbg1 2.04 mm to (174.0, 86.0)
- moved J1 0.17 mm to (176.7, 35.5)
- moved J2 0.17 mm to (123.9, 35.5)
- renumbered C25 to C20, C20 to C21, C21 to C22, C22 to C23, C23 to C24, C24 to C25, JP4 to JP1, JP13 to JP10, JP14 to JP11, JP15 to JP12, JP16 to JP13, JP17 to JP14, JP18 to JP15, JP19 to JP16, JP20 to JP17, JP21 to JP18, JP22 to JP19, JP5 to JP2, JP23 to JP20, JP24 to JP21, JP25 to JP22, JP26 to JP23, JP27 to JP24, JP28 to JP25, JP29 to JP26, JP30 to JP27, JP31 to JP28, JP32 to JP29, JP6 to JP3, JP33 to JP30, JP34 to JP31, JP35 to JP32, JP36 to JP33, JP37 to JP34, JP38 to JP35, JP39 to JP36, JP40 to JP37, JP41 to JP38, JP42 to JP39, JP7 to JP4, JP43 to JP40, JP44 to JP41, JP45 to JP42, JP46 to JP43, JP47 to JP44, JP48 to JP45, JP49 to JP46, JP50 to JP47, JP51 to JP48, JP52 to JP49, JP8 to JP5, JP53 to JP50, JP54 to JP51, JP55 to JP52, JP56 to JP53, JP9 to JP6, JP10 to JP7, JP11 to JP8, JP12 to JP9, R61 to R62, R62 to R63, R63 to R64, R64 to R65, R65 to R66, SYM6 to SYM1, SYM5 to SYM2, SYM4 to SYM3, SYM3 to SYM4, SYM1 to SYM5, SYM2 to SYM6
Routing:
- net +12V: track 79.7 -> 123.2 mm, vias 0 -> 1
- net +5V: track 180.9 -> 205.6 mm, vias 2 -> 3
- net +3.3V: track 383.8 -> 402.0 mm
- net L: track 413.8 -> 408.0 mm
- net TRGR1: track 144.2 -> 142.2 mm
- net Net-(3V3LED1-K): track 0.00 -> 1.87 mm
- net Net-(12VLED1-K): track 0.00 -> 1.87 mm
- net Net-(5VLED1-K): track 0.00 -> 1.84 mm
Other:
- board text added: "+12V"
- board text added: "+3V3"
- board text added: "+5V"
- board text added: "BOOT"
- board text added: "Cable dir"
- board text added: "JTAG"
- board text added: "PROG"
- board text added: "RESET"

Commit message: sent to production with fixes
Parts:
- removed D20: 1N4148, Diode_SMD:D_0805_2012Metric_Pad1.15x1.40mm_HandSolder
- removed H1, H2: MountingHole, MountingHole:MountingHole_3.5mm
- removed JP38, JP39, JP40, JP42, JP43, JP44, JP45, JP46, JP47, JP48, JP50, JP51, JP52, JP53: SolderJumper_2_Open, Jumper:SolderJumper-2_P1.3mm_Open_RoundedPad1.0x1.5mm
- removed J_JTAG1: FTSH-105-01-S-DV-K, OverlordCommon:FTSH-105-XX-YYY-DV-K
- removed J_JTAG3V3_1, J_PROG3V3_1: Conn_01x02_Pin, Connector_PinHeader_2.54mm:PinHeader_1x02_P2.54mm_Vertical
- removed R68: 147, Resistor_SMD:R_0805_2012Metric_Pad1.20x1.40mm_HandSolder
- added C26: 1uF, Capacitor_SMD:C_0805_2012Metric_Pad1.18x1.45mm_HandSolder, F.Cu at (175.9, 83.3)
- added J4: Conn_01x04_Pin, OverlordCommon:Solder_select_2x2, F.Cu at (75.9, 101.7)
- added J5: Conn_01x04_Pin, OverlordCommon:Solder_select_2x2, F.Cu at (64.3, 94.5)
- added J_JTAG2: FTSH-105-01-S-DV-K, OverlordCommon:FTSH-105-XX-YYY-DV-K, F.Cu at (45.8, 36.2)
- added R70: 147, Resistor_SMD:R_0805_2012Metric_Pad1.20x1.40mm_HandSolder, F.Cu at (174.4, 93.8)
- added U_LM317_2: LM317_SOT-223, Package_TO_SOT_SMD:SOT-223-3_TabPin2, F.Cu at (168.2, 85.7)
- moved SYM3 143.3 mm to (33.1, 94.8)
- moved SYM4 98.2 mm to (32.1, 106.3)
- moved D21 21.5 mm to (176.1, 86.8), turned to 0 degrees
- moved R1 8.08 mm to (170.9, 66.6)
- moved R2 8.08 mm to (170.8, 64.3)
- moved C1 8.08 mm to (176.1, 59.6)
- moved Q1 8.08 mm to (171.7, 56.2)
- moved Q2 8.08 mm to (177.3, 47.6)
- moved Q4 8.08 mm to (172.2, 47.6)
- moved D1 8.08 mm to (176.4, 64.9)
- moved Q3 8.08 mm to (175.8, 53.7)
- moved R3 8.08 mm to (175.8, 62.5)
- moved R4 8.08 mm to (170.1, 59.8)
- moved R5 8.08 mm to (172.4, 59.8)
- moved U1 8.08 mm to (170.2, 69.4)
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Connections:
- net Net-(U_LM317_1-ADJ) renamed V_ADJ
- C16 pad 1: Net-(D19-K) -> +12V
- D19 pad 1: Net-(D19-K) -> +12V
- D21 pad 1: Net-(D19-K) -> +5V
- D21 pad 2: +5V -> +3.3V
- DB9_IN1 pad 1: GND -> MB2_H
- DB9_IN1 pad 2: CAN_L -> MB2_L
- DB9_IN1 pad 4: MB2_L -> CAN_L
- DB9_IN1 pad 5: MB2_H -> GND
- DB9_IN1 pad 6: MB1_L -> +12V
- DB9_IN1 pad 7: CAN_H -> MB1_H
- DB9_IN1 pad 8: MB1_H -> CAN_H
- DB9_IN1 pad 9: +12V -> MB1_L
- J3 pad 8: unconnected-(J3-Pin_8-Pad8) -> CAN_H
- J3 pad 9: unconnected-(J3-Pin_9-Pad9) -> CAN_L
- JP41 pad 2: JTAG_TCK -> +3.3V
- JP49 pad 2: Net-(JP49-B) -> +3.3V
- J_PROG1 pad 1: Net-(JP48-B) -> ESP_EN
- J_PROG1 pad 3: Net-(JP50-B) -> UART_TX_0
- J_PROG1 pad 4: Net-(JP51-A) -> GND
- J_PROG1 pad 5: Net-(JP52-B) -> UART_RX_0
- J_PROG1 pad 6: Net-(JP53-A) -> ESP_IO0
- U_LM317_1 pad 3: Net-(D19-K) -> +12V
- U_TRS3232EIPWR1 pad 11: UART_TX_0 -> Net-(J5-Pin_1)
- U_TRS3232EIPWR1 pad 12: RS232_RX -> Net-(J5-Pin_2)
- U_TRS3232EIPWR1 pad 13: UART_RX_0 -> Net-(J4-Pin_1)
- U_TRS3232EIPWR1 pad 14: RS232_TX -> Net-(J4-Pin_2)
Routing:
- net Net-(JP38-A): track 34.1 -> 0.00 mm
- net L: track 408.0 -> 377.1 mm
- net GND: track 20.3 -> 48.2 mm, vias 341 -> 337
- net CAN_L: track 100.1 -> 127.7 mm
- net Net-(D19-K): track 20.5 -> 0.00 mm
- net CAN_H: track 98.3 -> 118.5 mm
- net UART_TX_0: track 125.7 -> 107.5 mm
- net Net-(JP41-A): track 4.16 -> 21.9 mm
- net +12V: track 123.2 -> 140.4 mm, vias 1 -> 2
- net UART_RX_0: track 116.0 -> 100.9 mm, vias 1 -> 2
- net Net-(J4-Pin_2): track 0.00 -> 14.7 mm
- net MB1_L: track 60.2 -> 47.7 mm
- net JTAG_TMS: track 40.4 -> 28.0 mm
- net Net-(J5-Pin_1): track 0.00 -> 10.8 mm
- net Net-(J4-Pin_1): track 0.00 -> 10.6 mm
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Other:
- board size 155.1 x 86.1 mm -> 155.7 x 86.3 mm
- board text added: "--- Overlord Dimmer --- Ver 1.1 Rev B Designed by"
- board text added: "3V3"
- board text added: "4N35"
- board text added: "CAN RX"
- board text added: "CAN TX"
- board text added: "CAN Termination"
- board text added: "DB9 IN"
- board text added: "DB9 OUT"
- board text added: "ESP32-S3-WROOM-1U-N16"
- board text added: "GND"
- board text added: "JTAG 3V3"
- board text added: "LM317"
- board text added: "PROG 3V3"
- board text added: "SN65HVD230"
- board text added: "TRS3232EIPWR"
- board text added: "TX RX"
- board text added: "UART"
- board text added: "USB"
- board text added: "Zero-cross detect"
- board text removed: "--- Overlord Dimmer --- Ver 1.1 Rev A Designed by"
